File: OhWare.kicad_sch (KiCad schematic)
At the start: 1 part, among them J3 Screw_Terminal_01x03

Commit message: Latest updates
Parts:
- renumbered J3 to J1
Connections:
- net GND: no longer J1.3 (Pin_3)
- new net Earth: J1.3 (Pin_3)
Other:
- sheet CAN ports: added CAN_RXD, CAN_TXD; removed none
- sheet Controller ports: added CAN1_Rx, CAN1_Tx, OTG_FS_DM, OTG_FS_DP, UART2_Rx, UART2_Tx; removed none
- sheet RS485 ports: added DI, RO; removed none
- sheet USB_FS ports: added USB_DM, USB_DP; removed none
- moved on the sheet: J1

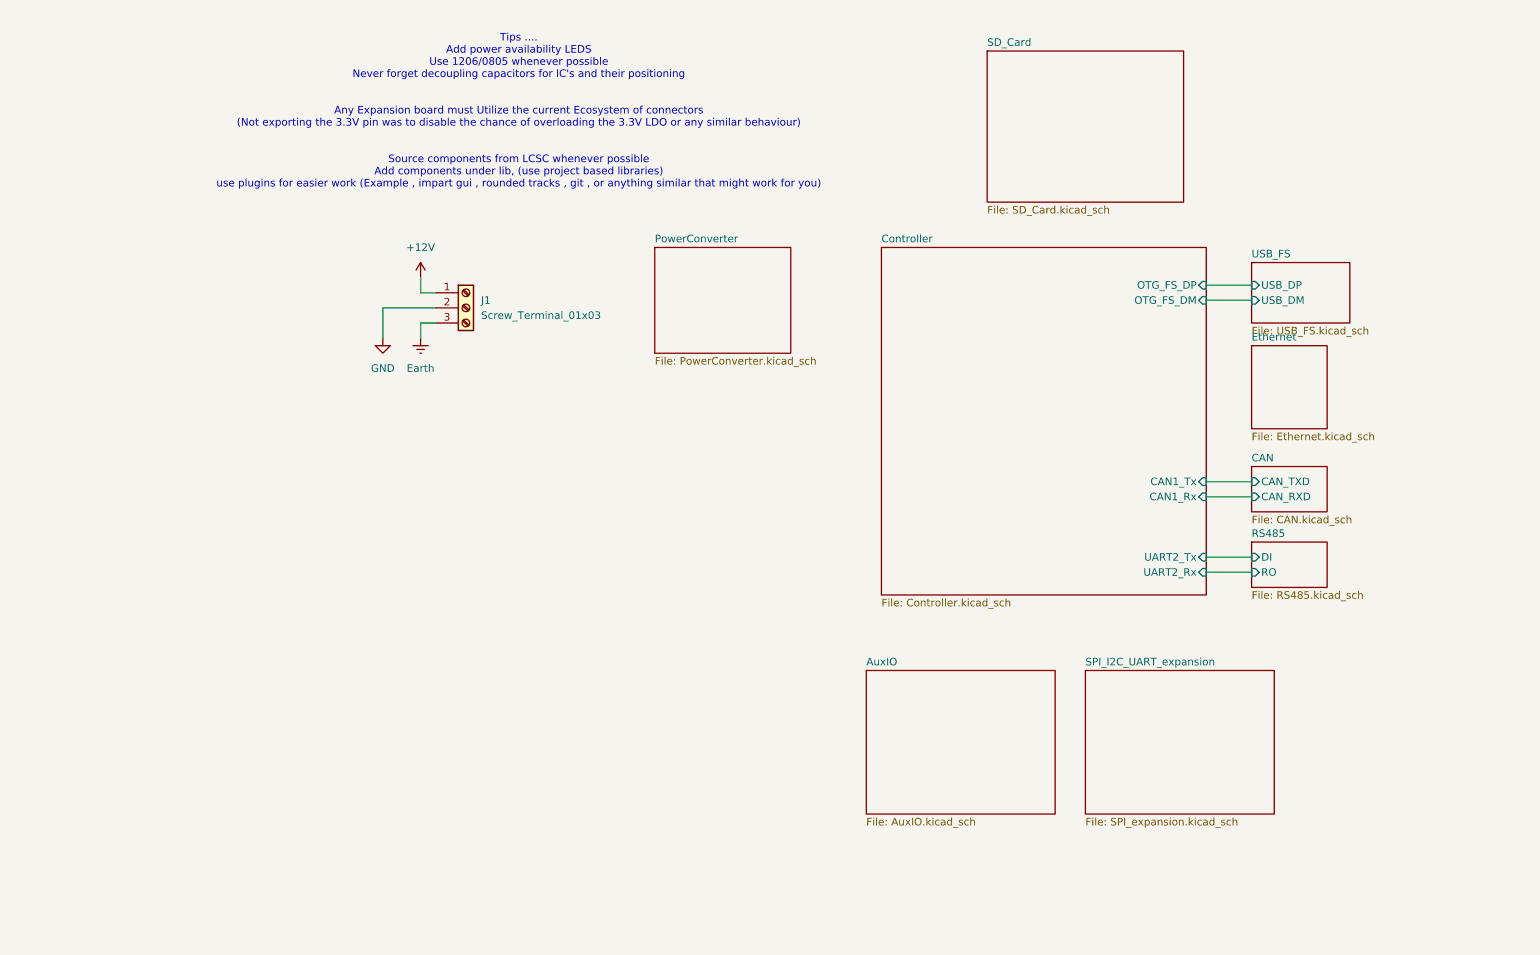
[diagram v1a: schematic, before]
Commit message: Latest changes (added SD , USB , CAN , RS485)
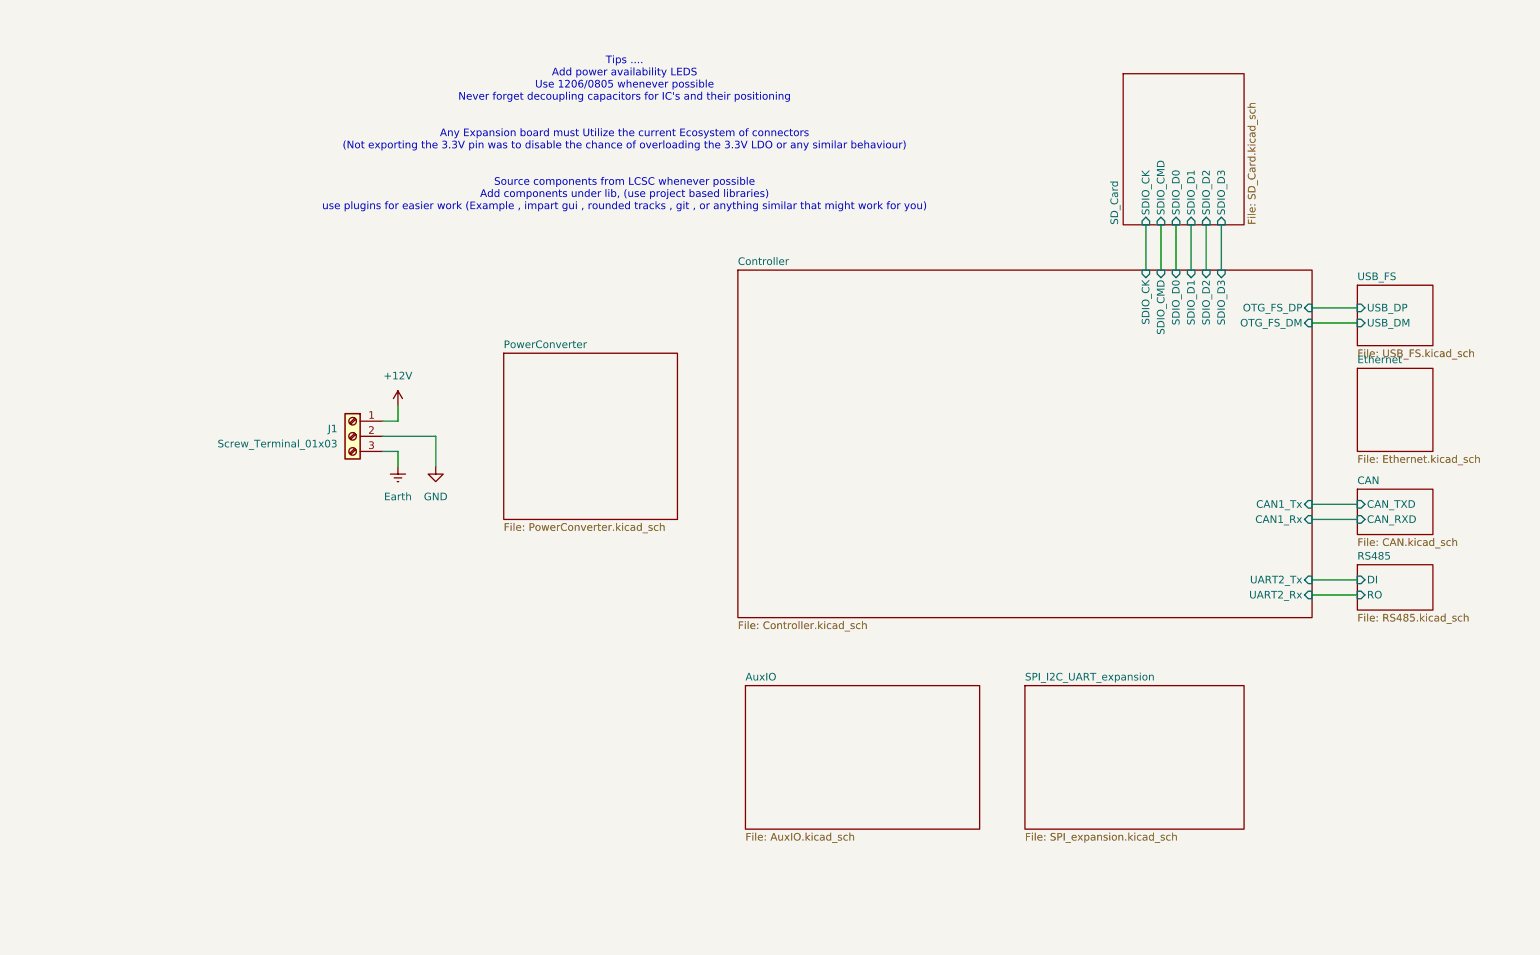
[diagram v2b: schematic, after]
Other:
- sheet Controller ports: added SDIO_CK, SDIO_CMD, SDIO_D0, SDIO_D1, SDIO_D2, SDIO_D3; removed none
- sheet SD_Card ports: added SDIO_CK, SDIO_CMD, SDIO_D0, SDIO_D1, SDIO_D2, SDIO_D3; removed none
- moved on the sheet: J1

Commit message: added Ethernet and SPI interface
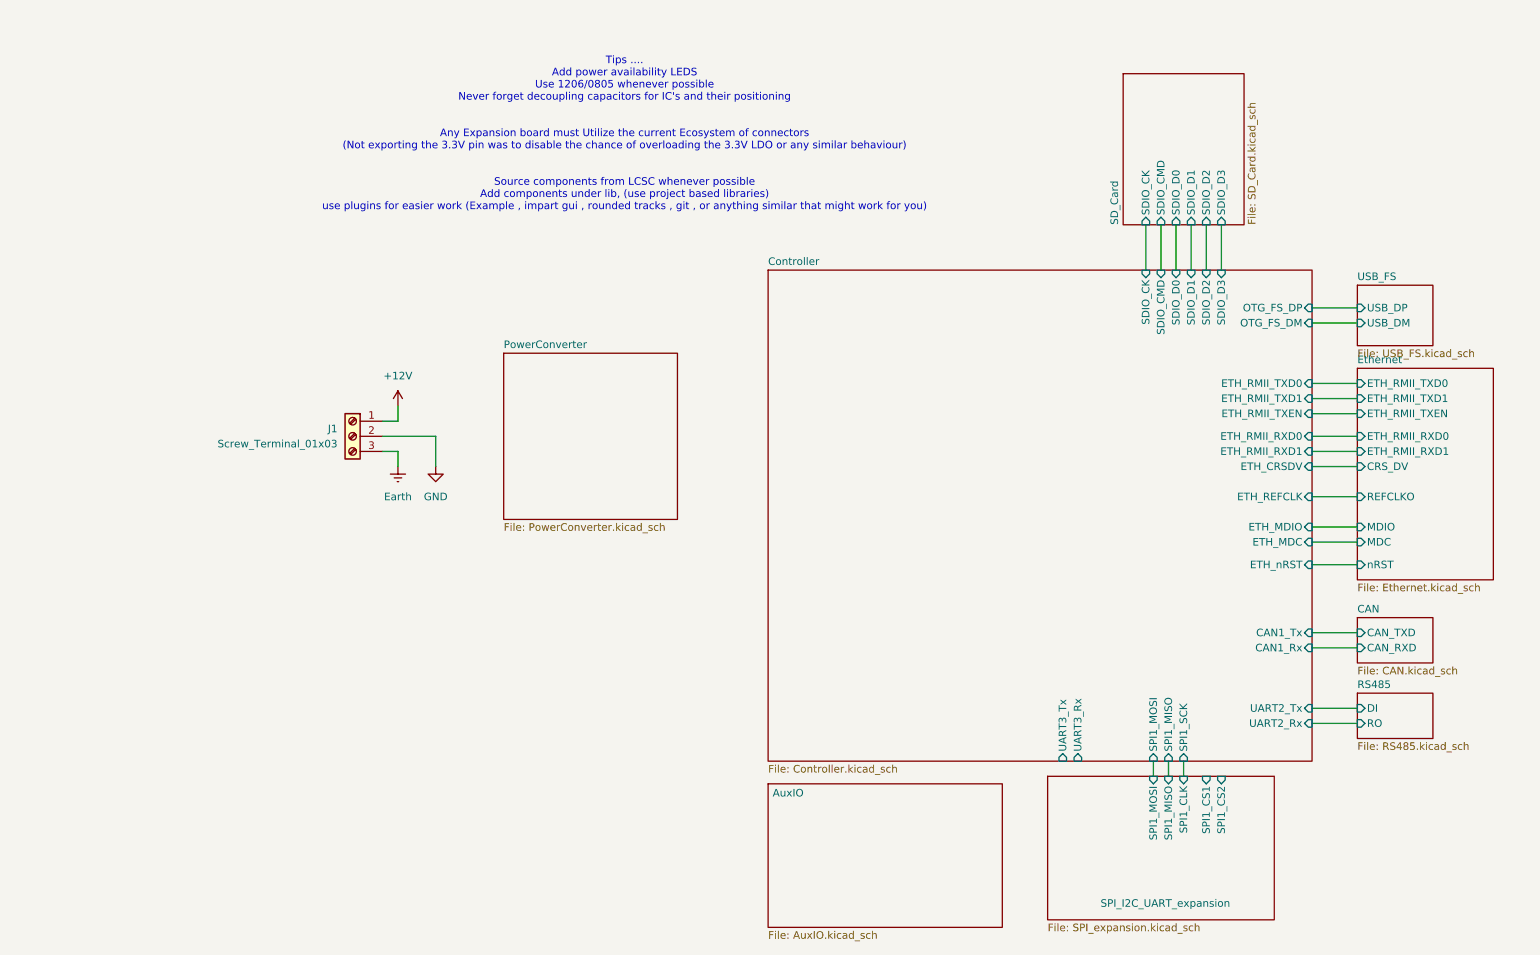
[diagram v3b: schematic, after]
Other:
- sheet Controller ports: added ETH_CRSDV, ETH_MDC, ETH_MDIO, ETH_REFCLK, ETH_RMII_RXD0, ETH_RMII_RXD1, ETH_RMII_TXD0, ETH_RMII_TXD1, ETH_RMII_TXEN, ETH_nRST, SPI1_MISO, SPI1_MOSI, SPI1_SCK, UART3_Rx, UART3_Tx; removed none
- sheet Ethernet ports: added CRS_DV, ETH_RMII_RXD0, ETH_RMII_RXD1, ETH_RMII_TXD0, ETH_RMII_TXD1, ETH_RMII_TXEN, MDC, MDIO, REFCLKO, nRST; removed none
- sheet SPI_I2C_UART_expansion ports: added SPI1_CLK, SPI1_CS1, SPI1_CS2, SPI1_MISO, SPI1_MOSI; removed none

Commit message: Schematic--Footprint link
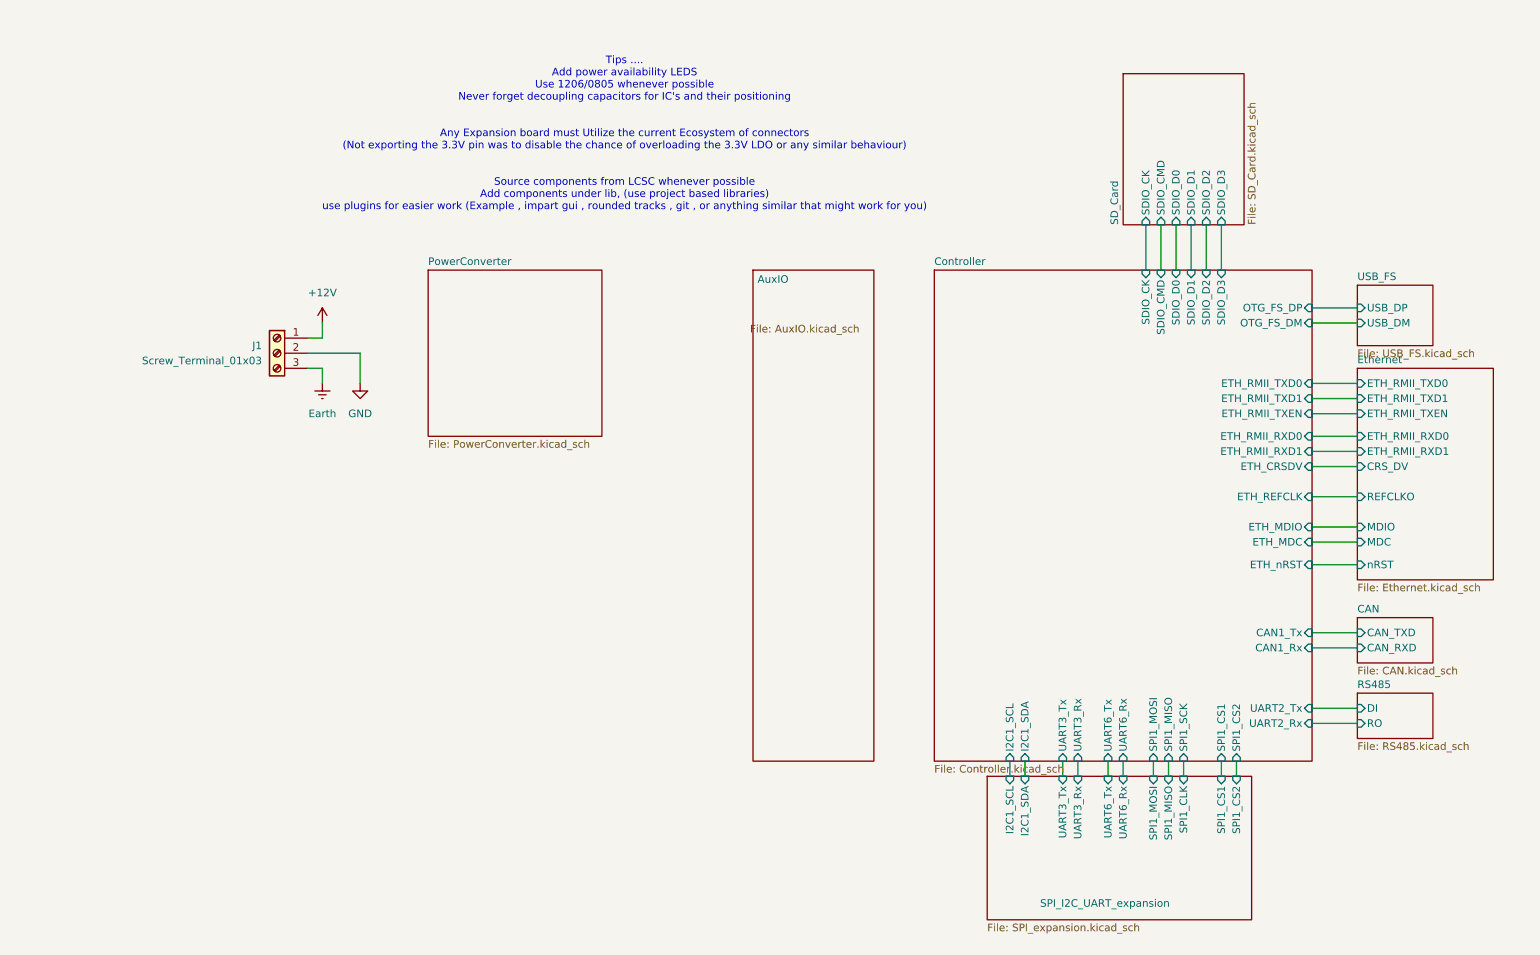
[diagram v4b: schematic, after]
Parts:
- J1: footprint (none) -> TerminalBlock_Phoenix:TerminalBlock_Phoenix_PT-1,5-3-5.0-H_1x03_P5.00mm_Horizontal
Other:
- sheet Controller ports: added I2C1_SCL, I2C1_SDA, SPI1_CS1, SPI1_CS2, UART6_Rx, UART6_Tx; removed none
- sheet SPI_I2C_UART_expansion ports: added I2C1_SCL, I2C1_SDA, UART3_Rx, UART3_Tx, UART6_Rx, UART6_Tx; removed none
- moved on the sheet: J1
